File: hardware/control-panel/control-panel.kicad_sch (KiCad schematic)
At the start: 51 parts, among them J2 Power/CAN, J4 Power/CAN, J5 SWD, J6 Conn_01x06_Pin, J7 ARGB, SW1 RotaryEncoder_Switch, SW2 RotaryEncoder_Switch, SW3 RotaryEncoder_Switch, SW4 RotaryEncoder_Switch, U1 TC1185-xCT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

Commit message: Update footprints to given in inventory
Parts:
- C11, C13, C2, C3, C4, C6: footprint Capacitor_SMD:C_0603_1608Metric_Pad1.08x0.95mm_HandSolder -> Capacitor_SMD:C_0805_2012Metric_Pad1.18x1.45mm_HandSolder
- L1: footprint Inductor_SMD:L_1008_2520Metric_Pad1.43x2.20mm_HandSolder -> Inductor_SMD:L_1210_3225Metric_Pad1.42x2.65mm_HandSolder
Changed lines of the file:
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@@
 			)
 		)
-		(property "Footprint" "Capacitor_SMD:C_0603_1608Metric_Pad1.08x0.95mm_HandSolder"
+		(property "Footprint" "Capacitor_SMD:C_0805_2012Metric_Pad1.18x1.45mm_HandSolder"
 			(at 206.0448 140.97 0)
 			(effects
@@
 			)
 		)
-		(property "Footprint" "Capacitor_SMD:C_0603_1608Metric_Pad1.08x0.95mm_HandSolder"
+		(property "Footprint" "Capacitor_SMD:C_0805_2012Metric_Pad1.18x1.45mm_HandSolder"
 			(at 133.6548 26.67 0)
 			(effects
@@
 			)
 		)
-		(property "Footprint" "Capacitor_SMD:C_0603_1608Metric_Pad1.08x0.95mm_HandSolder"
+		(property "Footprint" "Capacitor_SMD:C_0805_2012Metric_Pad1.18x1.45mm_HandSolder"
 			(at 186.3852 148.59 0)
 			(effects
@@
 			)
 		)
-		(property "Footprint" "Inductor_SMD:L_1008_2520Metric_Pad1.43x2.20mm_HandSolder"
+		(property "Footprint" "Inductor_SMD:L_1210_3225Metric_Pad1.42x2.65mm_HandSolder"
 			(at 113.03 24.13 0)
 			(effects
@@
 			)
 		)
-		(property "Footprint" "Capacitor_SMD:C_0603_1608Metric_Pad1.08x0.95mm_HandSolder"
+		(property "Footprint" "Capacitor_SMD:C_0805_2012Metric_Pad1.18x1.45mm_HandSolder"
 			(at 145.7452 35.56 0)
 			(effects
@@
 			)
 		)
-		(property "Footprint" "Capacitor_SMD:C_0603_1608Metric_Pad1.08x0.95mm_HandSolder"
+		(property "Footprint" "Capacitor_SMD:C_0805_2012Metric_Pad1.18x1.45mm_HandSolder"
 			(at 182.5752 35.56 0)
 			(effects
@@
 			)
 		)
-		(property "Footprint" "Capacitor_SMD:C_0603_1608Metric_Pad1.08x0.95mm_HandSolder"
+		(property "Footprint" "Capacitor_SMD:C_0805_2012Metric_Pad1.18x1.45mm_HandSolder"
 			(at 126.0348 26.67 0)
 			(effects

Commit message: Add notes
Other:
- note added: "Unless otherwise specified, the working voltage of all capacitors is 6.3V."
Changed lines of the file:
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@@
+		)
+	)
+	(text "Unless otherwise specified, the working voltage of all capacitors is 6.3V. "
+		(exclude_from_sim no)
+		(at 231.14 173.99 0)
+		(effects
+			(font
+				(size 1.8 1.8)
+			)
 		)
 	)

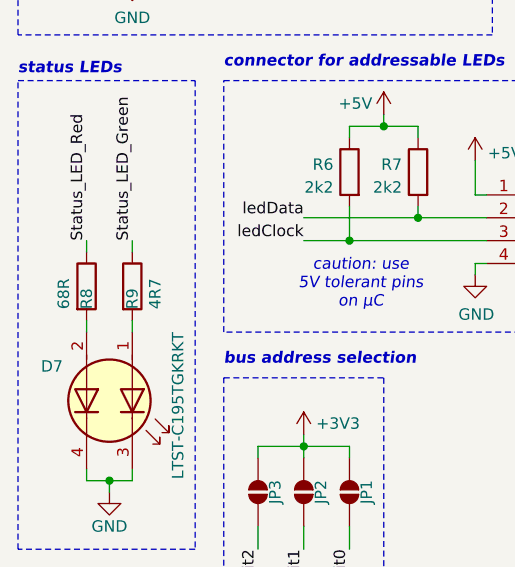
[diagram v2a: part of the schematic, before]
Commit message: Update some values
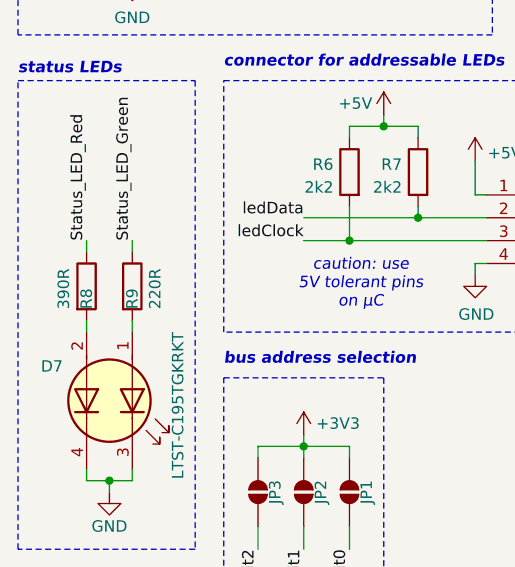
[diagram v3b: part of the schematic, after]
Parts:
- R8: value 68R -> 390R
- R9: value 4R7 -> 220R
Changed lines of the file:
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@@
 			)
 		)
-		(property "Value" "4R7"
+		(property "Value" "220R"
 			(at 30.48 138.43 90)
 			(effects
@@
 			)
 		)
-		(property "Value" "68R"
+		(property "Value" "390R"
 			(at 20.32 138.43 90)
 			(effects
